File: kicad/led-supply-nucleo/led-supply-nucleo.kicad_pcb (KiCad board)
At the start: 2 copper layers, 63 parts, among them Q1 BC848, Q2 BC848, Q3 IRLZ44N, Q4 IRLZ44N, Q5 IRLZ44N, Q6 IRLZ44N, Q7 IRLZ44N, Q8 IRLZ44N, U1 UCC27714D, U2 UCC27714D, U3 UCC27714D, U4 NUCLEO64-F411RE

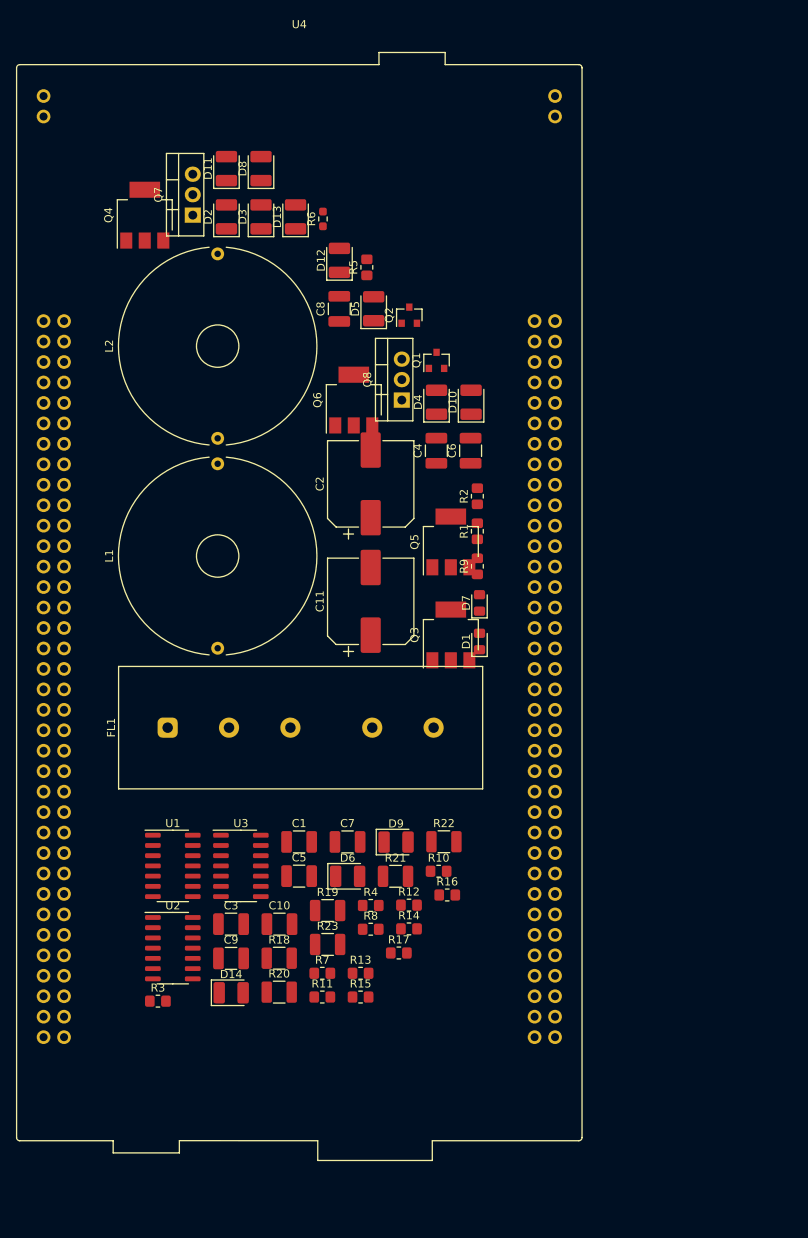
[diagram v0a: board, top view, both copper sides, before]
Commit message: Add Nucleo based board for prototyping.
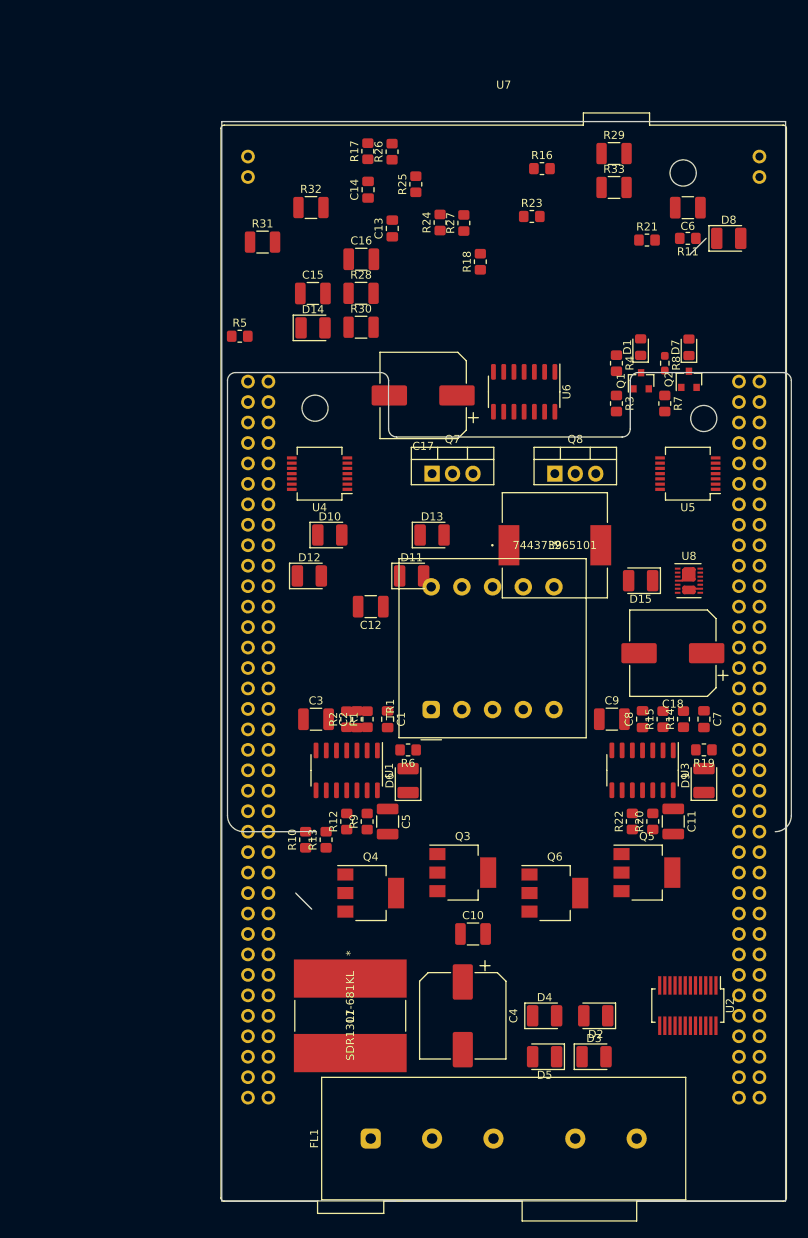
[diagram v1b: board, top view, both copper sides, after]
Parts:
- removed the C5 at (101.6, 142.7)
- added C1: C, Capacitor_SMD:C_0805_2012Metric_Pad1.18x1.45mm_HandSolder, F.Cu at (112.6, 123.2)
- added C13: C, Capacitor_SMD:C_0805_2012Metric_Pad1.18x1.45mm_HandSolder, F.Cu at (113.2, 62.3)
- added C14: C, Capacitor_SMD:C_0805_2012Metric_Pad1.18x1.45mm_HandSolder, F.Cu at (110.2, 57.5)
- added C18: CP, Capacitor_SMD:CP_Elec_10x12.5, F.Cu at (148.0, 115.0)
- added C2: C, Capacitor_SMD:C_0805_2012Metric_Pad1.18x1.45mm_HandSolder, F.Cu at (108.8, 123.2)
- added C7: C, Capacitor_SMD:C_0805_2012Metric_Pad1.18x1.45mm_HandSolder, F.Cu at (151.9, 123.2)
- added C8: C, Capacitor_SMD:C_0805_2012Metric_Pad1.18x1.45mm_HandSolder, F.Cu at (144.2, 123.2)
- added C9: CP, Capacitor_SMD:C_1210_3225Metric_Pad1.33x2.70mm_HandSolder, F.Cu at (140.4, 123.2)
- added D15: D_Schottky, Diode_SMD:D_1210_3225Metric_Pad1.42x2.65mm_HandSolder, F.Cu at (144.0, 106.0)
- added R1: R, Resistor_SMD:R_0805_2012Metric_Pad1.20x1.40mm_HandSolder, F.Cu at (110.0, 123.2)
- added R14: R, Resistor_SMD:R_0805_2012Metric_Pad1.20x1.40mm_HandSolder, F.Cu at (149.3, 123.2)
- added R15: R, Resistor_SMD:R_0805_2012Metric_Pad1.20x1.40mm_HandSolder, F.Cu at (146.8, 123.2)
- added R17: R, Resistor_SMD:R_0805_2012Metric_Pad1.20x1.40mm_HandSolder, F.Cu at (110.1, 52.7)
- added R18: R, Resistor_SMD:R_0805_2012Metric_Pad1.20x1.40mm_HandSolder, F.Cu at (124.1, 66.4)
- added R2: R, Resistor_SMD:R_0805_2012Metric_Pad1.20x1.40mm_HandSolder, F.Cu at (107.5, 123.2)
- added R24: R, Resistor_SMD:R_0805_2012Metric_Pad1.20x1.40mm_HandSolder, F.Cu at (119.1, 61.5)
- added R25: R, Resistor_SMD:R_0805_2012Metric_Pad1.20x1.40mm_HandSolder, F.Cu at (116.1, 56.8)
- added R26: R, Resistor_SMD:R_0805_2012Metric_Pad1.20x1.40mm_HandSolder, F.Cu at (113.1, 52.7)
- added R27: R, Resistor_SMD:R_0805_2012Metric_Pad1.20x1.40mm_HandSolder, F.Cu at (122.0, 61.6)
- added TR1: Wuerth_750343373, Transformer_THT:Transformer_Wuerth_750343373, F.Cu at (118.0, 122.0)
- added U2: ACS709xLFTR-6BB, Sensor_Current:Allegro_QSOP-24_3.9x8.7mm_P0.635mm, F.Cu at (149.9, 158.8)
- added U5: TL072, Package_SO:SSOP-14_5.3x6.2mm_P0.65mm, F.Cu at (149.9, 92.7)
- added U7: NUCLEO64-F411RE, Module:ST_Morpho_Connector_144_STLink, F.Cu at (95.2, 81.3)
- added U8: LT3032-12, Package_DFN_QFN:Linear_DE14MA, F.Cu at (150.0, 106.0)
- L1: value L -> SDR1307-681KL; footprint Inductor_THT:L_Radial_D24.4mm_P22.90mm_muRATA_1400series -> kicad-footprint:SDR1307-681KL
- L2: value L -> 744373965101; footprint Inductor_THT:L_Radial_D24.4mm_P22.90mm_muRATA_1400series -> kicad-footprint:744373965101
- Q3, Q4, Q5, Q6: footprint Package_TO_SOT_SMD:SOT-223 -> Package_TO_SOT_SMD:SOT-223-3_TabPin2
- U4: value NUCLEO64-F411RE -> TL072; footprint Module:ST_Morpho_Connector_144_STLink -> Package_SO:SSOP-14_5.3x6.2mm_P0.65mm
- moved D3 112.2 mm to (138.2, 165.1), turned to 0 degrees
- moved D2 109.3 mm to (138.4, 160.0), turned to 180 degrees
- moved R21 100.5 mm to (144.8, 63.7)
- moved R29 100.5 mm to (140.7, 53.0)
- moved R33 100.5 mm to (140.7, 57.2)
- moved D5 95.3 mm to (132.1, 165.1), turned to 180 degrees
- moved R16 92.9 mm to (131.8, 54.8)
- moved R23 92.9 mm to (130.5, 60.8)
- moved Q4 88.7 mm to (110.5, 144.8), turned to 0 degrees
- moved R28 83.2 mm to (109.3, 70.3)
- moved R30 83.2 mm to (109.3, 74.5)
- moved D14 83.2 mm to (103.3, 74.6)
- moved C15 83.2 mm to (103.3, 70.3)
- moved C16 83.2 mm to (109.3, 66.1)
- moved R5 83.2 mm to (94.2, 75.7)
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- renumbered C6 to C10, C7 to C11, C8 to C12, C9 to C15, C10 to C16, C11 to C17, C1 to C3, C2 to C4, C3 to C5, C4 to C6, R8 to R10, R9 to R11, R10 to R12, R11 to R13, R12 to R16, R13 to R19, R14 to R20, R15 to R21, R16 to R22, R17 to R23, R18 to R28, R19 to R29, R1 to R3, R20 to R30, R21 to R31, R22 to R32, R23 to R33, R2 to R4, R3 to R5, R4 to R6, R5 to R7, R6 to R8, R7 to R9, U2 to U3, U3 to U6
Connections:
- C15 pad 1: Net-(C9-Pad1) -> Net-(C15-Pad1)
- C17 pad 1: /power-converter/V_SENSE_O -> /power-converter/V_O
- C17 pad 2: Net-(C11-Pad2) -> Net-(C17-Pad2)
- C4 pad 1: Net-(C2-Pad1) (its old number) -> /power-converter/V_RECTIFIED
- C4 pad 2: Net-(C11-Pad2) -> Net-(C4-Pad2)
- C6 pad 2: Net-(C11-Pad2) -> Net-(C4-Pad2)
- D10 pad 1: /power-converter/V_SENSE_O -> /power-converter/V_O
- D11 pad 2: Net-(C11-Pad2) -> Net-(C17-Pad2)
- D12 pad 1: /power-converter/V_SENSE_O -> /power-converter/V_O
- D13 pad 2: Net-(C11-Pad2) -> Net-(C17-Pad2)
- D2 pad 1: Net-(C2-Pad1) (its old number) -> /power-converter/V_RECTIFIED
- D3 pad 2: Net-(C11-Pad2) -> Net-(C4-Pad2)
- D4 pad 1: Net-(C2-Pad1) (its old number) -> /power-converter/V_RECTIFIED
- D5 pad 2: Net-(C11-Pad2) -> Net-(C4-Pad2)
- L1 pad 2: Net-(C2-Pad1) (its old number) -> /power-converter/V_RECTIFIED
- L2 pad 1: Net-(L2-Pad1) -> /power-converter/COM_PAIR_3
- Q4 pad 3: Net-(C11-Pad2) -> Net-(C4-Pad2)
- Q6 pad 3: Net-(C11-Pad2) -> Net-(C4-Pad2)
- Q7 pad 1: Net-(Q7-Pad1) -> /power-converter/G_Q5
- Q7 pad 2: /power-converter/V_SENSE_O -> /power-converter/V_O
- Q7 pad 3: Net-(L2-Pad1) -> /power-converter/COM_PAIR_3
- Q8 pad 1: Net-(Q8-Pad1) -> /power-converter/G_Q6
- Q8 pad 2: Net-(L2-Pad1) -> /power-converter/COM_PAIR_3
- Q8 pad 3: Net-(C11-Pad2) -> Net-(C17-Pad2)
- R11 pad 2: Net-(C11-Pad2) -> Net-(C4-Pad2)
- R13 pad 2: Net-(R11-Pad2) -> GND
- R16 pad 2: Net-(C5-Pad1) (its old number) -> Net-(C9-Pad1)
- R19 pad 2: Net-(C5-Pad1) (its old number) -> Net-(C9-Pad1)
- R23 pad 2: Net-(R17-Pad2) (its old number) -> GND
- R28 pad 2: Net-(C9-Pad1) -> Net-(C15-Pad1)
- R29 pad 2: Net-(C9-Pad1) -> Net-(C15-Pad1)
- R33 pad 2: Net-(R23-Pad2) -> GND
- U1 pad 5: Net-(R11-Pad2) -> GND
- U3 pad 5: Net-(R17-Pad2) (its old number) -> GND
- U3 pad 7: Net-(U2-Pad7) -> Net-(C9-Pad1)
- U4 pad 1: Net-(U4-Pad1) -> /power-converter/V_SENSE_I
- U4 pad 10: Net-(U4-Pad10) -> (no net)
- U4 pad 11: Net-(U4-Pad11) -> (no net)
- U4 pad 12: Net-(U4-Pad12) -> (no net)
- U4 pad 13: Net-(U4-Pad13) -> (no net)
- U4 pad 14: Net-(U4-Pad14) -> (no net)
- U4 pad 2: Net-(U4-Pad2) -> /power-converter/V_SENSE_I
- U4 pad 4: Net-(U4-Pad4) -> (no net)
- U4 pad 5: Net-(U4-Pad5) -> (no net)
- U4 pad 6: Net-(U4-Pad6) -> (no net)
- U4 pad 7: Net-(U4-Pad7) -> (no net)
- U4 pad 8: Net-(U4-Pad8) -> (no net)
- U4 pad 9: Net-(U4-Pad9) -> (no net)
- U6 pad 5: Net-(R23-Pad2) -> GND
- U6 pad 7: Net-(U3-Pad7) -> Net-(C15-Pad1)
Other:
- board outline added: 70.7 x 134 mm
- copper layers 2 -> 4
- board text added: "STM32 Morpho"
- board text added: "®©®"
